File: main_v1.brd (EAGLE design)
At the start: 160 x 84.8 mm, 41 parts, among them IC1 MEGA8-P, IC2 7805TV

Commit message: Prettify
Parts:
- removed GOLD_ORB_SM2: OSHWLOGO_GOLD_ORB_MED, bfl:OSHW1
- removed GOLD_ORB_SM3: OSHWLOGO_GOLD_ORB_SM, bfl:OSHW2
- moved GOLD_ORB_SM1 110.5 mm to (35.6, -1.27)
- moved C4 7.24 mm to (33.0, 38.7)
- moved C12 1.90 mm to (33.0, 63.5)
- renumbered SV1 to H1, SV2 to H2, SV3 to H3, SV4 to H4, U$1 to IC5, U$2 to IC6, U$3 to IC4
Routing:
- net GND: track 247.0 -> 250.9 mm
- net VCC: track 170.1 -> 169.1 mm
- added copper zone on layer 1, net GND
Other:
- board size 160 x 84.8 mm -> 83.8 x 82.9 mm
- board text added: "KJ-22"
- board text added: "YT KJ-22 Oct 2016"

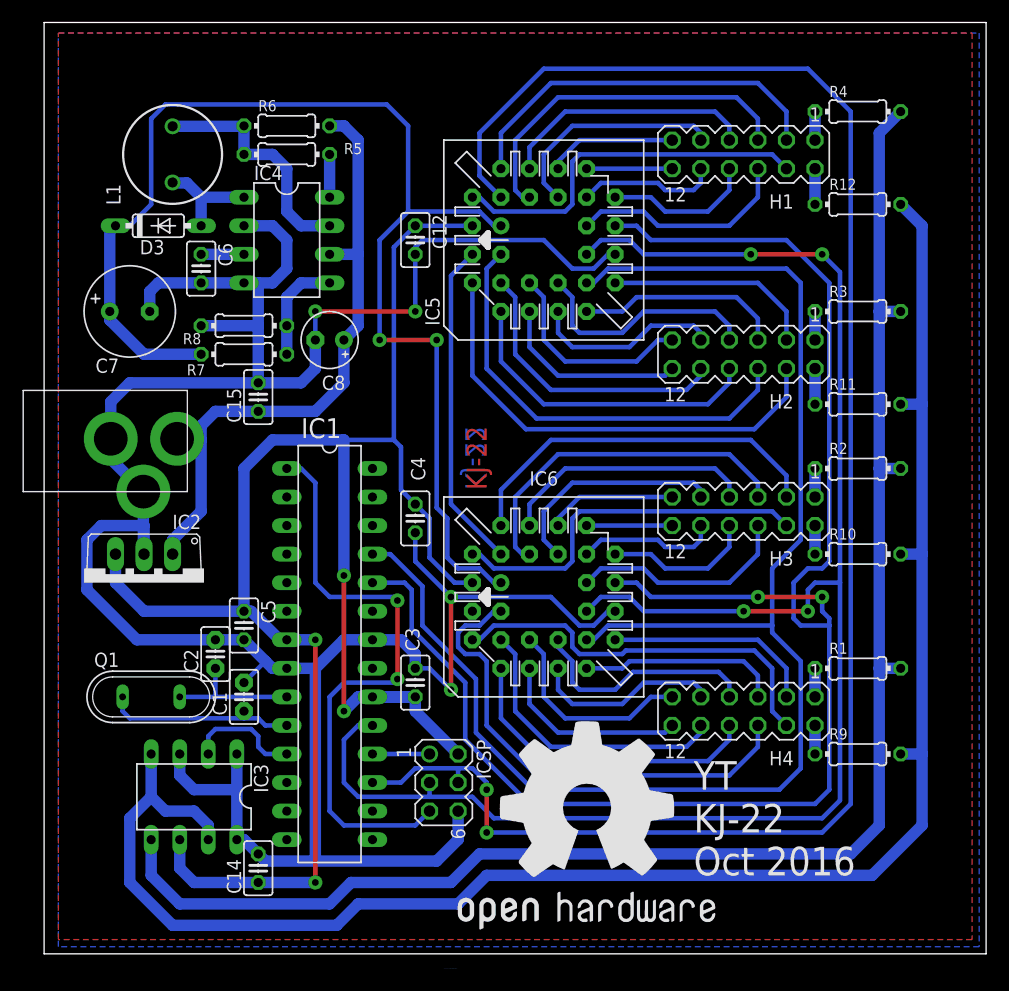
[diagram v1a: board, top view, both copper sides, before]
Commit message: Holes and logo fix
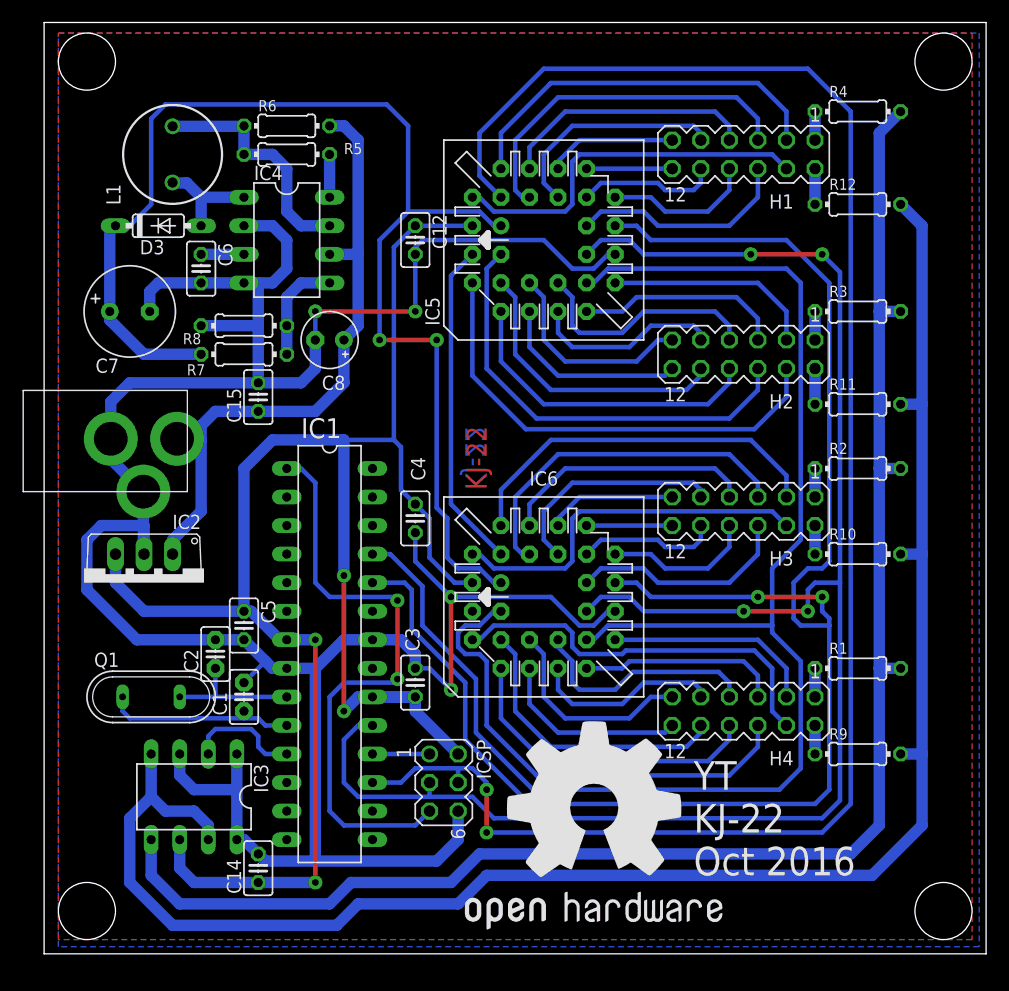
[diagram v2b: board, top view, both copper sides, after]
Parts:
- moved GOLD_ORB_SM1 19.3 mm to (48.9, 12.7)
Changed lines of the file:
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@@
 <layer number="43" name="vRestrict" color="2" fill="10" visible="yes" active="yes"/>
 <layer number="44" name="Drills" color="7" fill="1" visible="no" active="yes"/>
-<layer number="45" name="Holes" color="7" fill="1" visible="no" active="yes"/>
+<layer number="45" name="Holes" color="7" fill="1" visible="yes" active="yes"/>
 <layer number="46" name="Milling" color="3" fill="1" visible="no" active="yes"/>
 <layer number="47" name="Measures" color="7" fill="1" visible="no" active="yes"/>
@@
 <text x="39.37" y="41.275" size="1.778" layer="1" font="vector" rot="R90">KJ-22</text>
 <text x="37.465" y="41.275" size="1.778" layer="16" font="vector" rot="MR90">KJ-22</text>
+<hole x="3.81" y="3.81" drill="5.08"/>
+<hole x="3.81" y="79.375" drill="5.08"/>
+<hole x="80.01" y="79.375" drill="5.08"/>
+<hole x="80.01" y="3.81" drill="5.08"/>
 </plain>
 <attributes>
@@
 <attribute name="VALUE" x="22.987" y="57.023" size="1.27" layer="27" ratio="10" rot="R180"/>
 </element>
-<element name="GOLD_ORB_SM1" library="bfl" package="OSHW0" value="OSHWLOGO_GOLD_ORB_LG" x="35.56" y="-1.27"/>
+<element name="GOLD_ORB_SM1" library="bfl" package="OSHW0" value="OSHWLOGO_GOLD_ORB_LG" x="48.895" y="12.7"/>
 <element name="IC2" library="linear" package="TO220V" value="7805TV" x="8.89" y="33.02" rot="R180"/>
 <element name="DCIN" library="adafruit" package="PJ-102A" value="2.1MMJACKTHM" x="2.54" y="45.72" rot="R90"/>

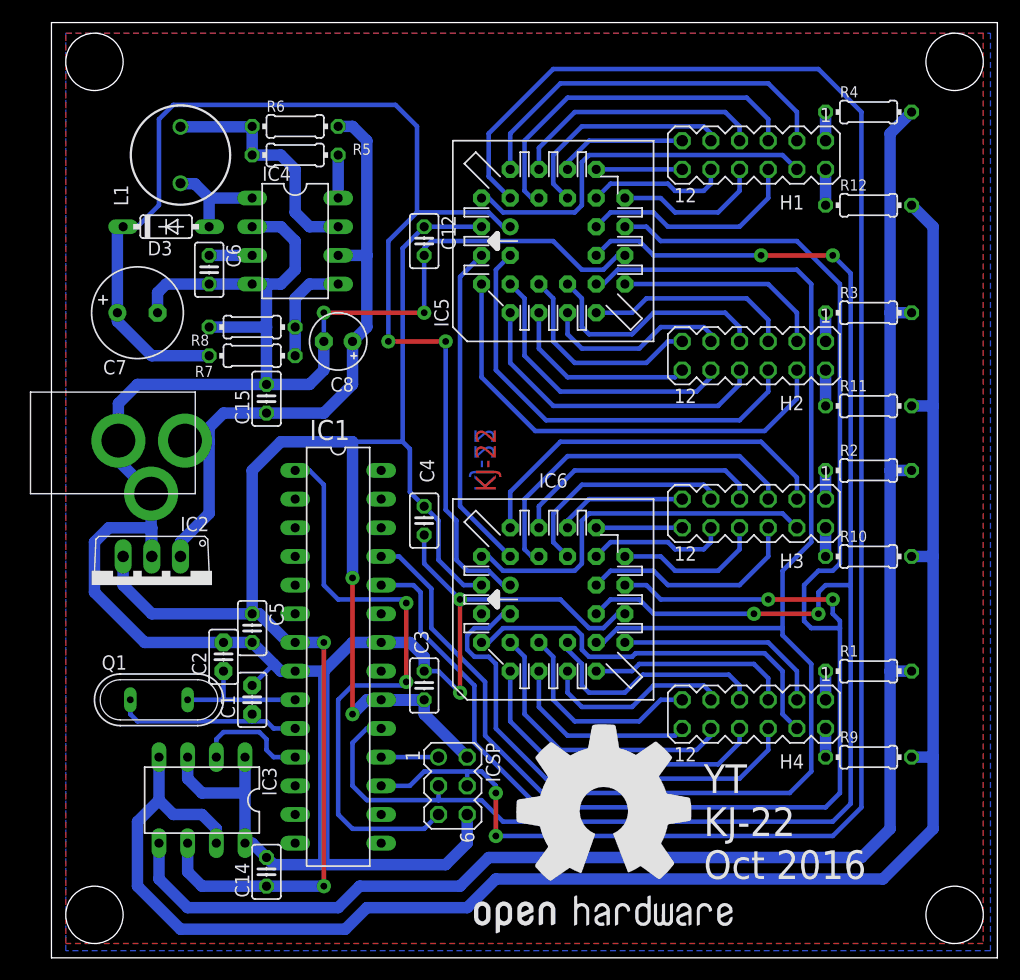
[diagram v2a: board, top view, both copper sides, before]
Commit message: Added better OSHW logo
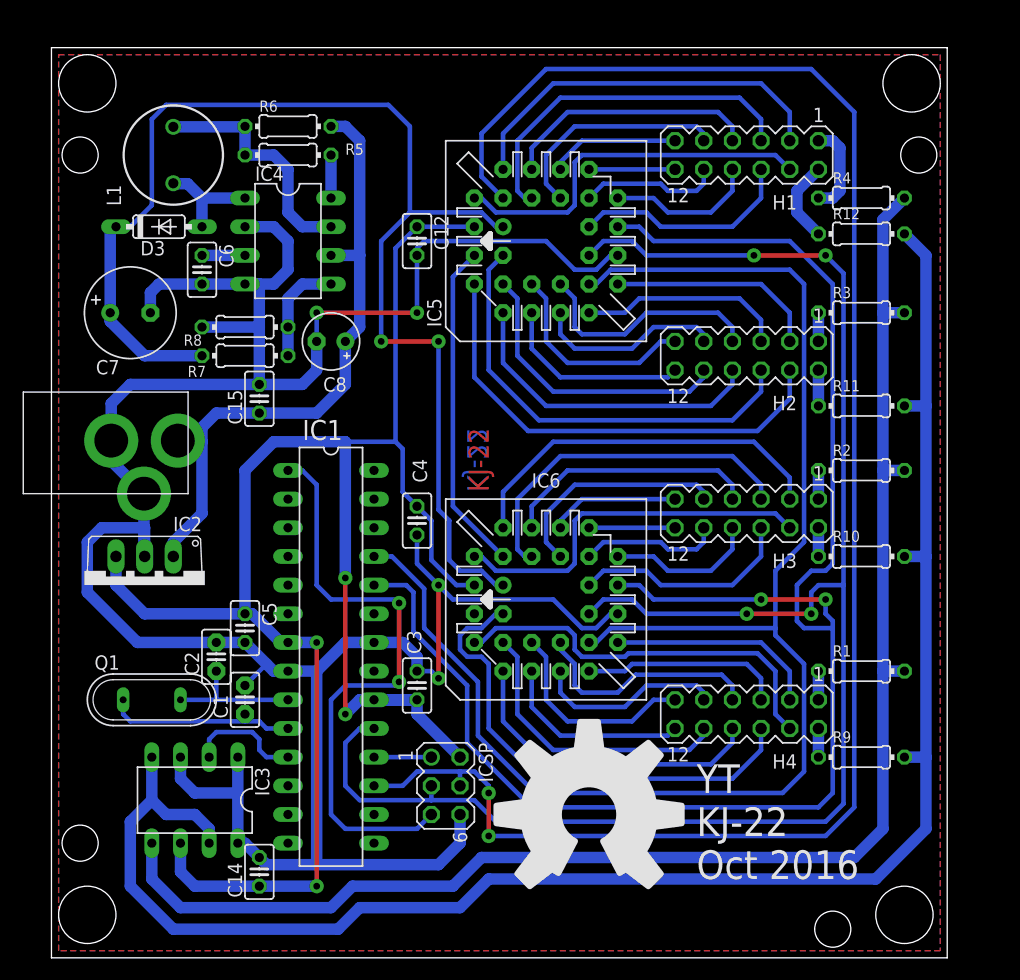
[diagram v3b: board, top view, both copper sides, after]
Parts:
- removed GOLD_ORB_SM1: OSHWLOGO_GOLD_ORB_LG, bfl:OSHW0
- moved R4 7.65 mm to (71.8, 67.3)
- moved R12 2.62 mm to (71.8, 64.1)
- moved C12 0.64 mm to (32.4, 63.5)
- moved C3 0.64 mm to (32.4, 24.1)
- moved C4 0.64 mm to (32.4, 38.7)
- moved IC5 0.64 mm to (43.8, 63.5)
- moved IC6 0.64 mm to (43.8, 31.8)
- moved ICSP 0.64 mm to (34.9, 15.2)
- moved R1 0.64 mm to (71.8, 25.4)
- moved R10 0.64 mm to (71.8, 35.6)
- moved R11 0.64 mm to (71.8, 48.9)
- moved R2 0.64 mm to (71.8, 43.2)
- moved R3 0.64 mm to (71.8, 57.1)
- moved R9 0.64 mm to (71.8, 17.8)
- moved C1 0.64 mm to (17.1, 22.9)
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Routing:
- net HT+: track 141.9 -> 134.3 mm
- net HT+1: track 2.54 -> 8.15 mm
- net HT-1: track 3.17 -> 7.29 mm
- net HT-: track 157.1 -> 154.6 mm
- net GND: track 250.9 -> 249.1 mm
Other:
- board size 83.8 x 82.9 mm -> 79.4 x 80.6 mm

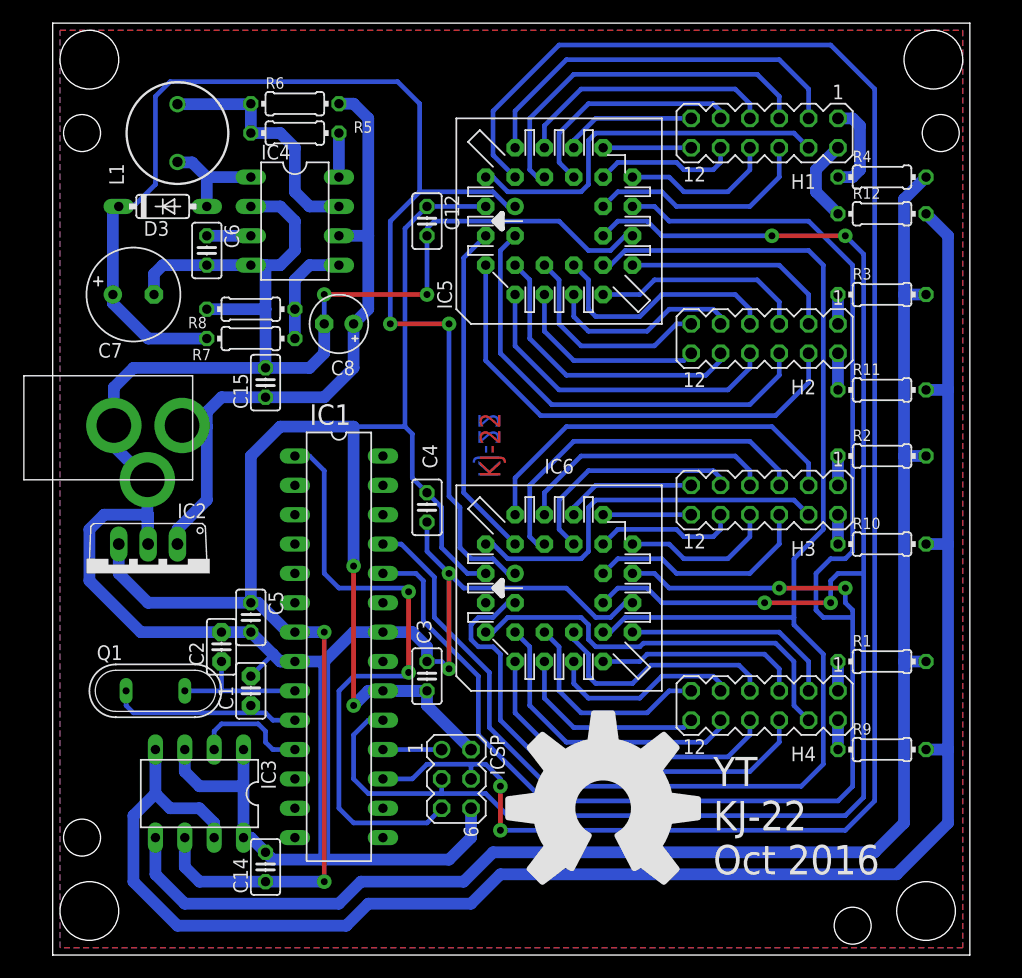
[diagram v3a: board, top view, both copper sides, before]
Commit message: Fix OSHPark complaints
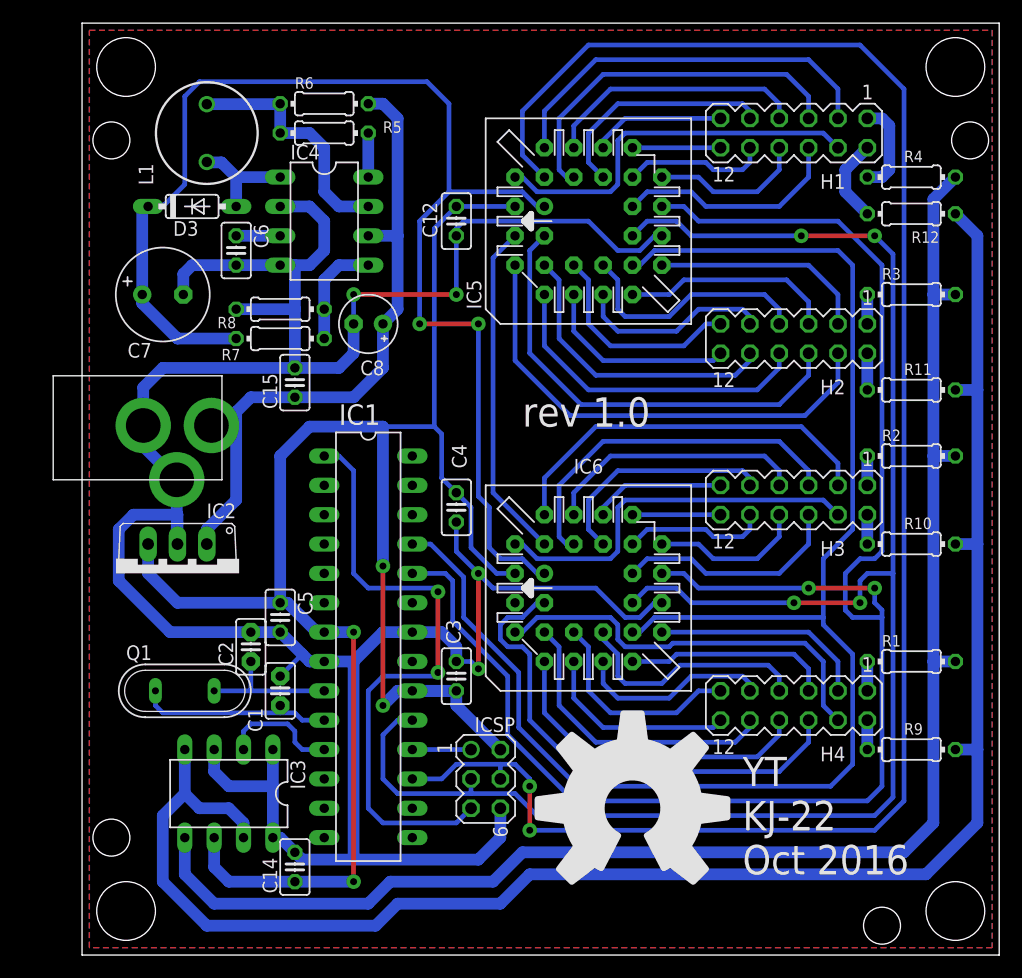
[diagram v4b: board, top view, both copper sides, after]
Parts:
- moved H1 2.54 mm to (64.1, 71.1)
- moved H2 2.54 mm to (64.1, 53.3)
- moved H3 2.54 mm to (64.1, 39.4)
- moved H4 2.54 mm to (64.1, 21.6)
- moved ICSP 2.54 mm to (37.5, 15.2)
- moved R1 2.54 mm to (74.3, 25.4)
- moved R10 2.54 mm to (74.3, 35.6)
- moved R11 2.54 mm to (74.3, 48.9)
- moved R12 2.54 mm to (74.3, 64.1)
- moved R2 2.54 mm to (74.3, 43.2)
- moved R3 2.54 mm to (74.3, 57.1)
- moved R4 2.54 mm to (74.3, 67.3)
- moved R9 2.54 mm to (74.3, 17.8)
- moved IC4 2.54 mm to (23.5, 63.5)
- moved R5 2.54 mm to (23.5, 71.1)
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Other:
- board text added: "rev 1.0"
- board text removed: "KJ-22"
